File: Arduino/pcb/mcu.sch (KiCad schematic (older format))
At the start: 27 parts, among them J9 FTDI, SW2 Reset Button, U2 ATMEGA328P-AU, U3 24LC64, U5 74AHC1G08, Y1 20 Mhz Crystal

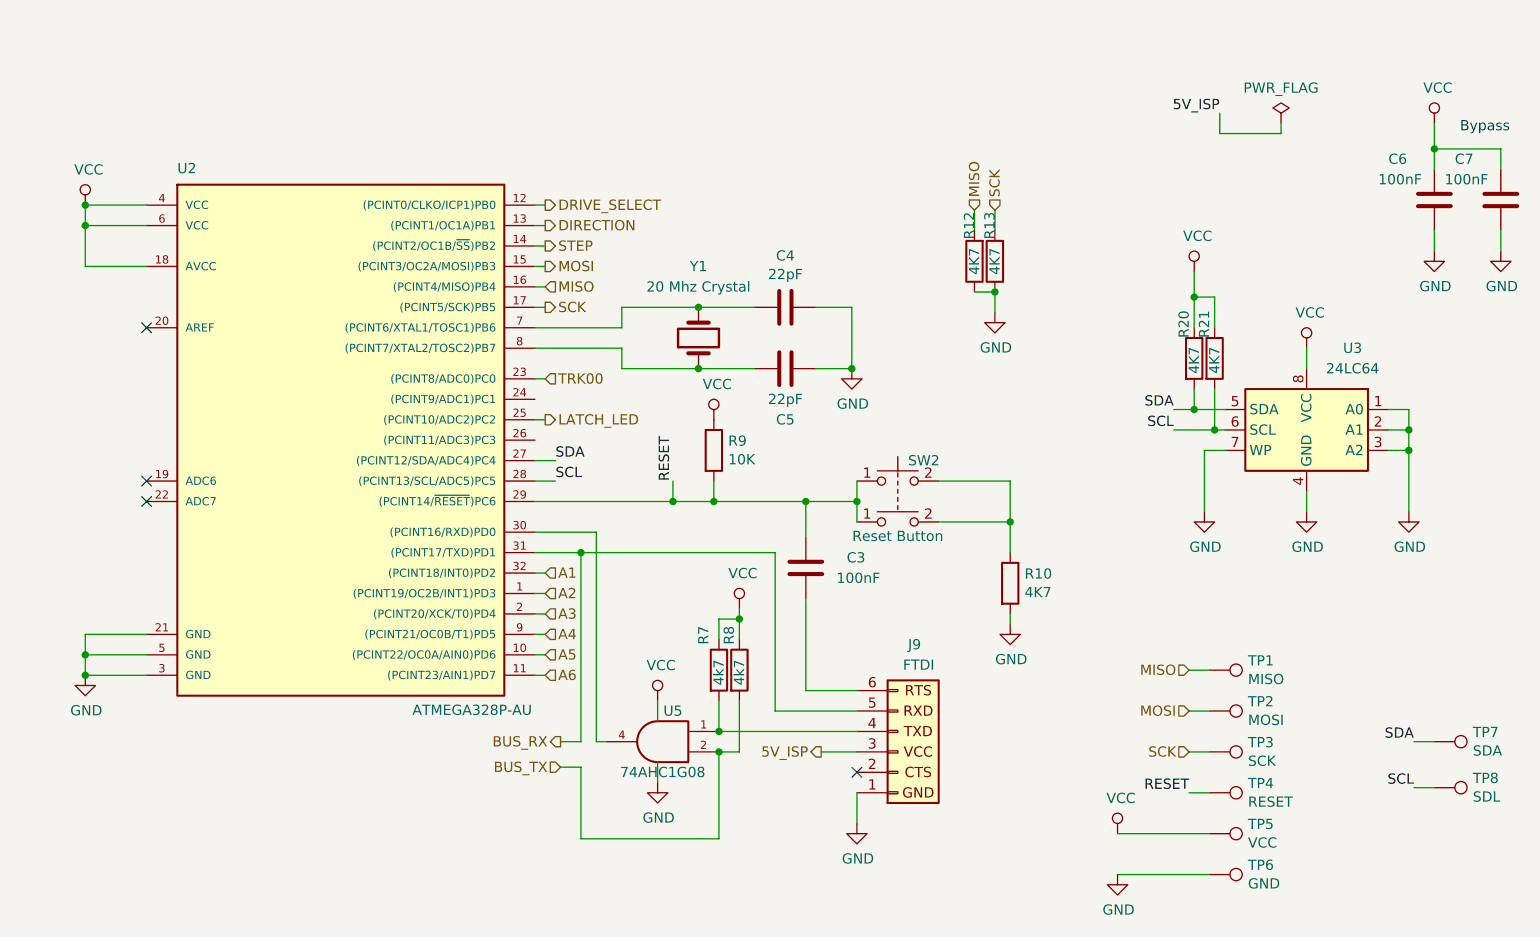
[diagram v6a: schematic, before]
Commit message: pcb / led: remove hc595 shift register / connect led directly
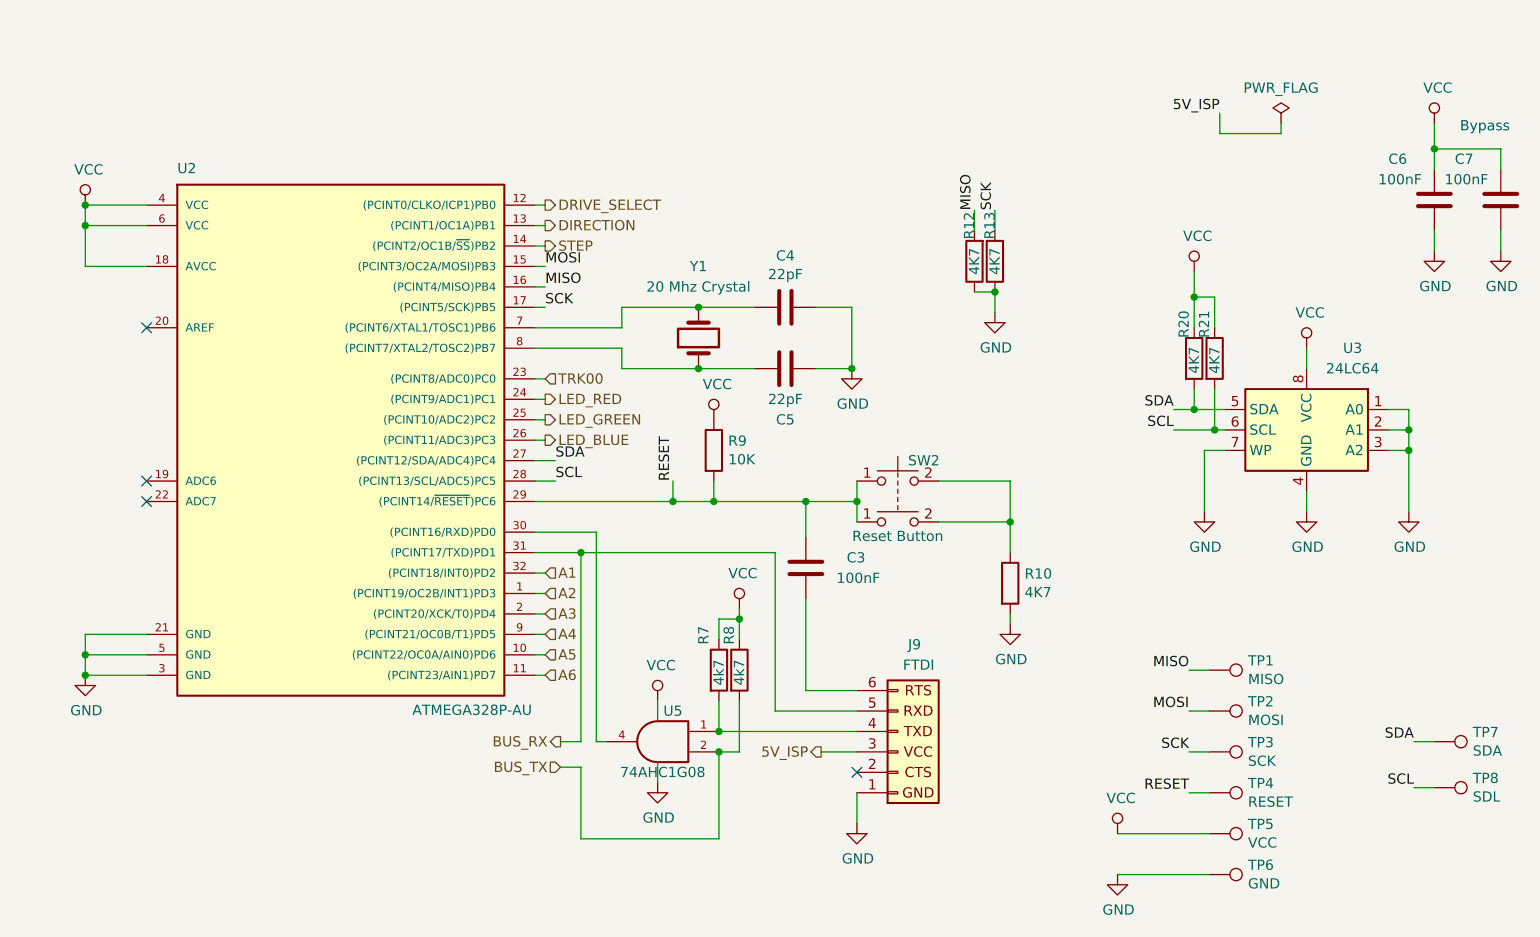
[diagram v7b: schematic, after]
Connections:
- net LED_RED: now reaches U2.24 ((PCINT9/ADC1)PC1)
- net LED_BLUE: now reaches U2.26 ((PCINT11/ADC3)PC3)
- net LATCH_LED renamed LED_GREEN
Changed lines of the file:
@@
 NoConn ~ 3925 3825
 Wire Wire Line
-	5825 3525 5875 3525
-Wire Wire Line
 	5825 3175 6250 3175
 Wire Wire Line
@@
 Text HLabel 5875 2675 2    50   Output ~ 0
 STEP
-Text HLabel 5875 2875 2    50   Input ~ 0
-MISO
-Text HLabel 5875 2975 2    50   Output ~ 0
-SCK
 Text HLabel 5875 3325 2    50   Input ~ 0
 TRK00
@@
 Wire Wire Line
 	7975 2500 7975 2600
-Text HLabel 7975 2500 1    50   Input ~ 0
-MISO
-Text HLabel 8075 2500 1    50   Input ~ 0
-SCK
 $Comp
 L Device:R R?
@@
 Wire Wire Line
 	9100 3675 9100 3975
-Text HLabel 5875 2775 2    50   Output ~ 0
-MOSI
 $Comp
 L Device:C C?
@@
 Wire Wire Line
 	9125 5350 9025 5350
-Text HLabel 9025 4750 0    50   Input ~ 0
-MISO
-Text HLabel 9025 4950 0    50   Input ~ 0
-MOSI
-Text HLabel 9025 5150 0    50   Input ~ 0
-SCK
 Wire Wire Line
 	6500 3825 6500 3925
@@
 Text HLabel 5875 4275 2    50   Input ~ 0
 A1
-Text HLabel 5875 3525 2    50   Output ~ 0
-LATCH_LED
 $Comp
 L power:GND #PWR?
@@
 	8075 2900 8075 3000
 Connection ~ 8075 2900
+Text HLabel 5875 3425 2    50   Output ~ 0
+LED_RED
+Text HLabel 5875 3525 2    50   Output ~ 0
+LED_GREEN
+Text HLabel 5875 3625 2    50   Output ~ 0
+LED_BLUE
+Wire Wire Line
+	5825 3425 5875 3425
+Wire Wire Line
+	5825 3525 5875 3525
+Wire Wire Line
+	5825 3625 5875 3625
+Text Label 5875 2875 0    50   ~ 0
+MISO
+Text Label 5875 2775 0    50   ~ 0
+MOSI
+Text Label 5875 2975 0    50   ~ 0
+SCK
+Text Label 9025 4750 2    50   ~ 0
+MISO
+Text Label 9025 4950 2    50   ~ 0
+MOSI
+Text Label 9025 5150 2    50   ~ 0
+SCK
+Text Label 7975 2500 1    50   ~ 0
+MISO
+Text Label 8075 2500 1    50   ~ 0
+SCK
 $EndSCHEMATC

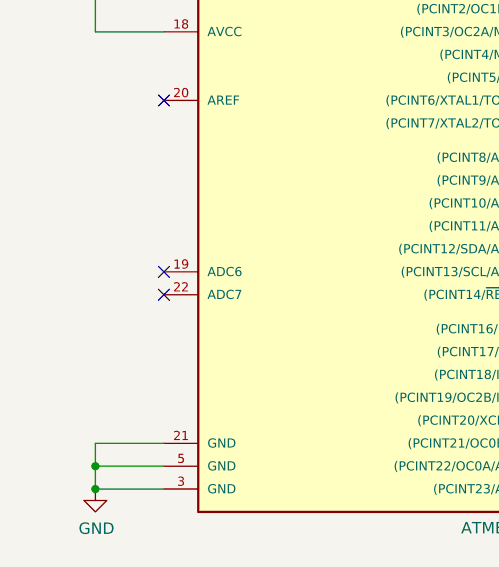
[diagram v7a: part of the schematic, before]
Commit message: pcb: route RS485 control pins
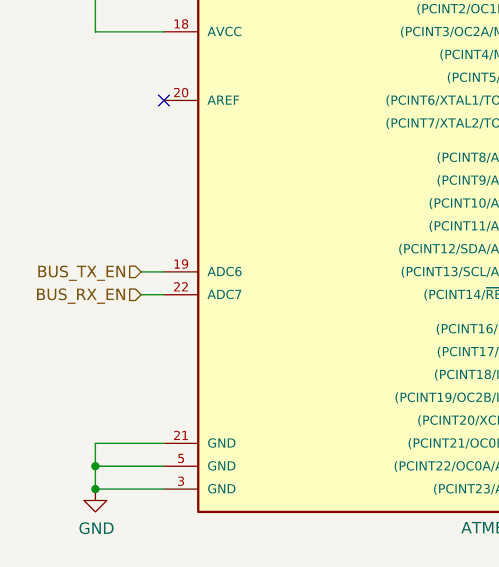
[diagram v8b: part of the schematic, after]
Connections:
- net BUS_TX_EN: now reaches U2.19 (ADC6)
- net BUS_RX_EN: now reaches U2.22 (ADC7)
- no-connect marks 4 -> 2
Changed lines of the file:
@@
 $Descr A4 11693 8268
 encoding utf-8
-Sheet 6 6
+Sheet 4 6
 Title ""
 Date ""
@@
 Comment4 ""
 $EndDescr
-NoConn ~ 3925 3925
-NoConn ~ 3925 3825
 Wire Wire Line
 	5825 3175 6250 3175
@@
 Text Label 8075 2500 1    50   ~ 0
 SCK
+Text HLabel 3825 3825 0    50   Input ~ 0
+BUS_TX_EN
+Text HLabel 3825 3925 0    50   Input ~ 0
+BUS_RX_EN
+Wire Wire Line
+	3825 3825 3925 3825
+Wire Wire Line
+	3825 3925 3925 3925
 $EndSCHEMATC
